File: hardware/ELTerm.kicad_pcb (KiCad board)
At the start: 2 copper layers, 81.6 x 44.5 mm, 31 parts, among them J1 Barrel_Jack_Switch, J2 Conn_02x10_Odd_Even, J3 Conn_01x02, J4 Mini-DIN-6, J5 Conn_02x03_Odd_Even, J6 Conn_01x02, J7 DB9_Male_MountingHoles, SW1 SW_Push, U1 SY8120, U2 Pico, U3 MAX3232, U4 NC7WZ16P6X

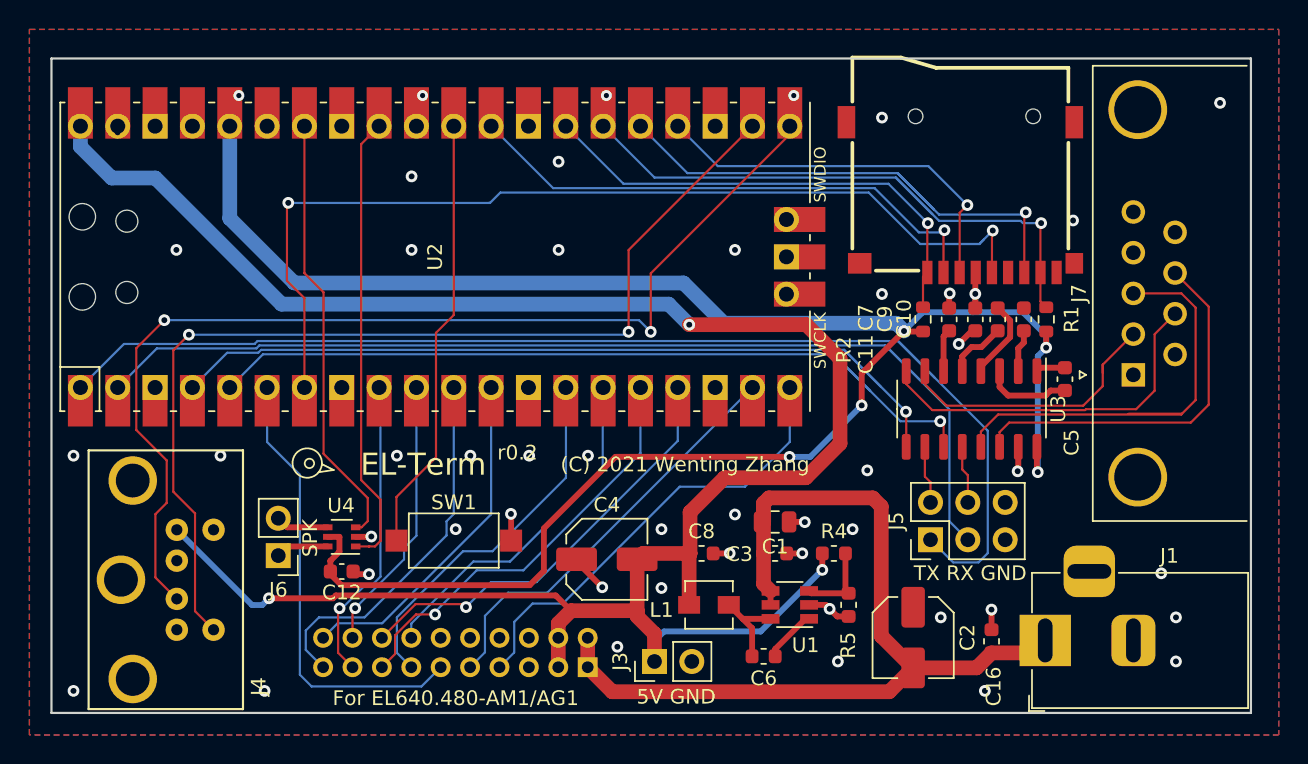
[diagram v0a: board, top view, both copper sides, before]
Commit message: Adapt EL screen to sharp LJ64
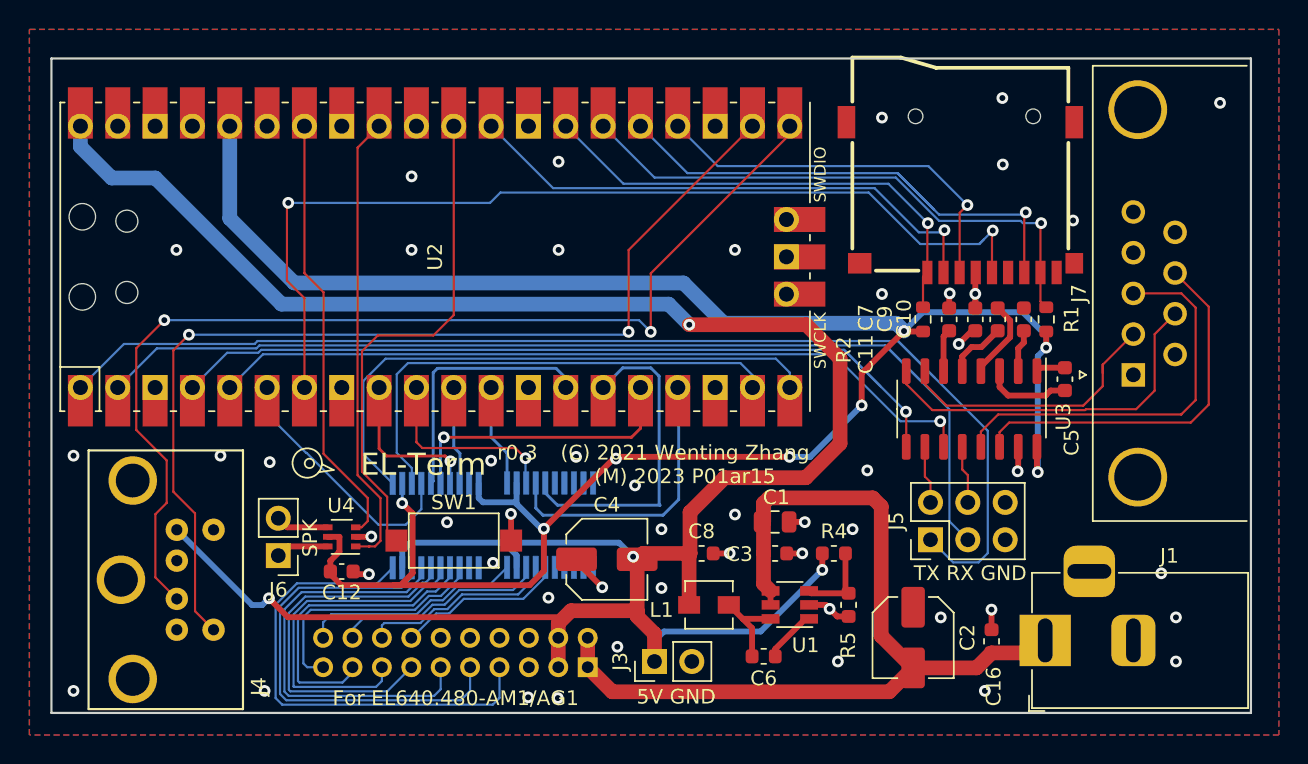
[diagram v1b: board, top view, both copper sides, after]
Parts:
- added U5: TXB0108PWR, TXB0108PWR:SOP65P640X120-20N, B.Cu at (101.6, 111.8)
- added U6: TXB0108PWR, TXB0108PWR:SOP65P640X120-20N, B.Cu at (109.4, 111.7)
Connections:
- J2 pad 11: /VCLK -> Net-(J2-Pin_11)
- J2 pad 13: /LD3 -> Net-(J2-Pin_13)
- J2 pad 14: /LD2 -> Net-(J2-Pin_14)
- J2 pad 15: /LD1 -> Net-(J2-Pin_15)
- J2 pad 16: /LD0 -> Net-(J2-Pin_16)
- J2 pad 17: /UD3 -> Net-(J2-Pin_17)
- J2 pad 18: /UD2 -> Net-(J2-Pin_18)
- J2 pad 19: /UD1 -> Net-(J2-Pin_19)
- J2 pad 20: /UD0 -> Net-(J2-Pin_20)
- J2 pad 7: /VSYNC -> Net-(J2-Pin_7)
- J2 pad 9: /HSYNC -> Net-(J2-Pin_9)
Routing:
- net Net-(J2-Pin_7): track 0.00 -> 33.1 mm
- net Net-(J2-Pin_9): track 0.00 -> 31.4 mm
- net Net-(J2-Pin_11): track 0.00 -> 28.9 mm
- net Net-(J2-Pin_13): track 0.00 -> 25.6 mm
- net Net-(J2-Pin_15): track 0.00 -> 23.7 mm
- net Net-(J2-Pin_17): track 0.00 -> 20.9 mm
- net +5V: track 148.8 -> 168.5 mm, vias 3 -> 4
- net /UD1: track 25.5 -> 6.71 mm
- net +3V3: track 136.7 -> 154.8 mm, vias 7 -> 9
- net Net-(J2-Pin_19): track 0.00 -> 17.0 mm
- net /UD0: track 23.5 -> 7.14 mm
- net Net-(J2-Pin_20): track 0.00 -> 15.1 mm
- net Net-(J2-Pin_18): track 0.00 -> 14.5 mm
- net Net-(J2-Pin_16): track 0.00 -> 13.3 mm
- net /VCLK: track 30.9 -> 17.6 mm
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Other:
- board text added: "(C) 2021 Wenting Zhang (M) 2023 P01ar15"
- board text added: "r0.3"
- board text removed: "(C) 2021 Wenting Zhang"
- board text removed: "r0.2"
